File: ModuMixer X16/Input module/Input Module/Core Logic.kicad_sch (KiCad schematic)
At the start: 57 parts, among them Q1 MMBT2222A, U1 AMS1117-1.8, U2 LM324, U3 TLV320AIC3100, U4 STM32F405RGTx, U5 4016

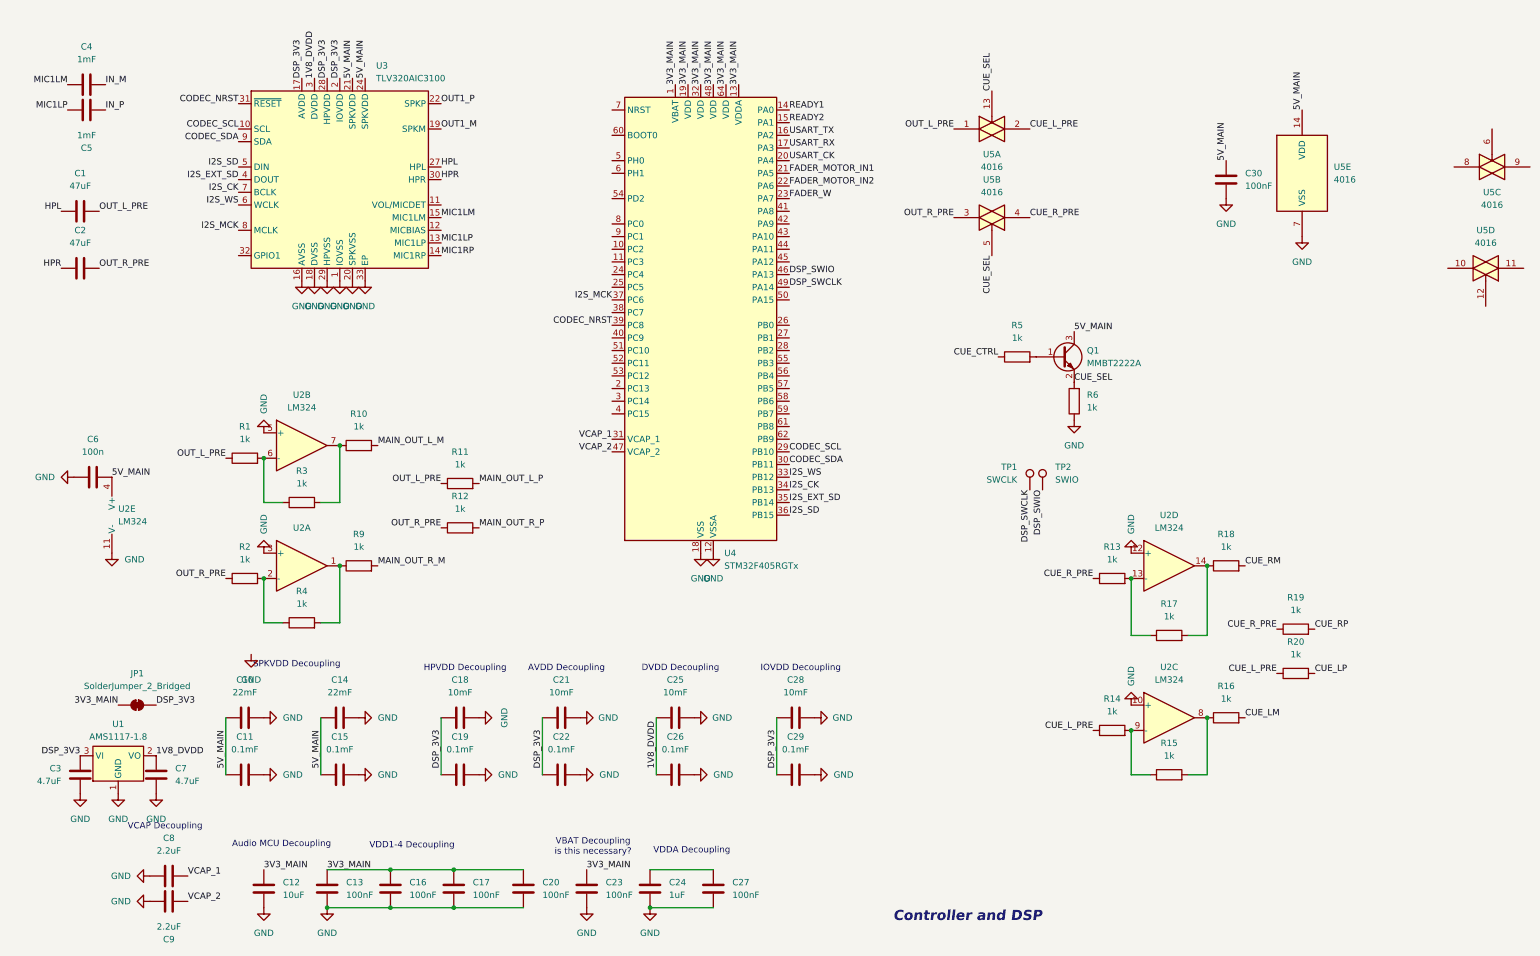
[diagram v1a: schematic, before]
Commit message: MCU replacement finished
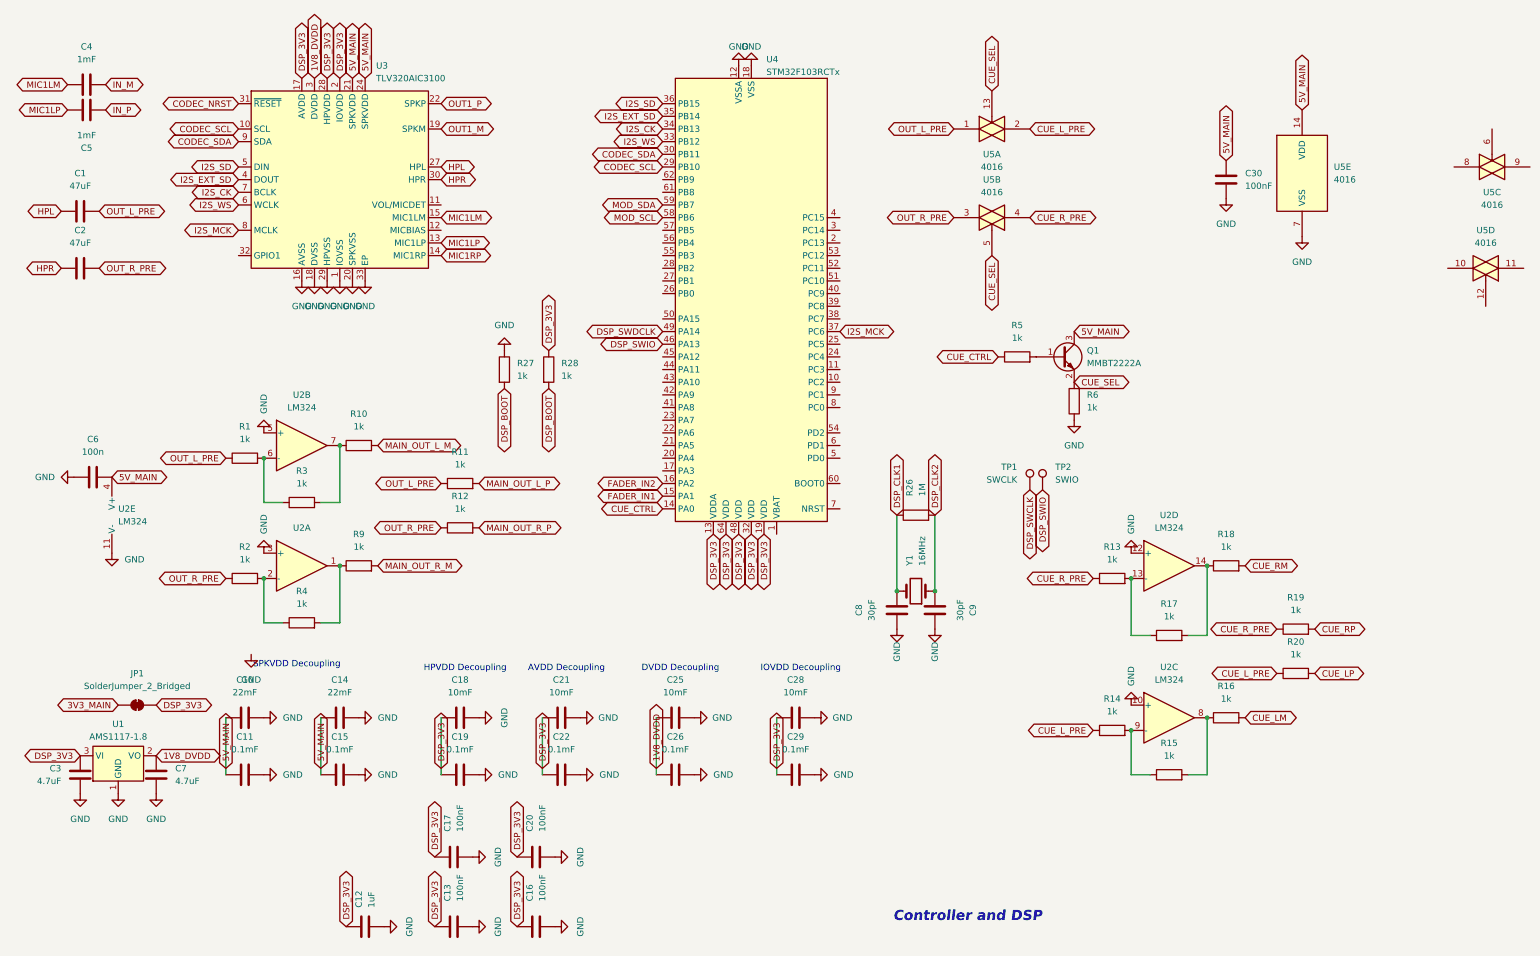
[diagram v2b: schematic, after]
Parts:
- removed C23, C27: 100nF, Capacitor_SMD:C_0603_1608Metric, symbol Device:C
- removed C24: 1uF, Capacitor_SMD:C_0603_1608Metric, symbol Device:C
- removed U4: STM32F405RGTx, Package_QFP:LQFP-64_10x10mm_P0.5mm, symbol MCU_ST_STM32F4:STM32F405RGTx
- added R26: 1M, Resistor_SMD:R_0603_1608Metric, symbol Device:R
- added R27, R28: 1k, Resistor_SMD:R_0603_1608Metric, symbol Device:R
- added U4: STM32F103RCTx, Package_QFP:LQFP-64_10x10mm_P0.5mm, symbol MCU_ST_STM32F1:STM32F103RCTx
- added Y1: 16MHz, Crystal:Crystal_HC49-U_Vertical, symbol Device:Crystal
- C12: value 10uF -> 1uF
- C8, C9: value 2.2uF -> 30pF
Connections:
- net VCAP_1 is gone; now on net GND: C8.2
- net 3V3_MAIN: no longer C12.2, C13.2, C16.2, C17.2, C20.2
- net CODEC_SCL: now also U4.29 (PB10)
- net CODEC_SDA: now also U4.30 (PB11)
- net CUE_CTRL: now also U4.14 (PA0)
- net DSP_3V3: now also C12.1, C13.1, C16.1, C17.1, C20.1, R28.1, U4.13 (VDDA), U4.19 (VDD), U4.32 (VDD), U4.48 (VDD), U4.64 (VDD)
- net DSP_SWIO: now also U4.46 (PA13)
- net GND: now also C12.2, C13.2, C16.2, C17.2, C20.2, R27.1, U4.12 (VSSA), U4.18 (VSS), U4.31 (VSS), U4.47 (VSS), U4.63 (VSS); no longer C12.1, C13.1, C16.1, C17.1, C20.1, C8.1
- net I2S_CK: now also U4.34 (PB13)
- net I2S_EXT_SD: now also U4.35 (PB14)
- net I2S_MCK: now also U4.37 (PC6)
- net I2S_SD: now also U4.36 (PB15)
- net I2S_WS: now also U4.33 (PB12)
- net VCAP_2 renamed DSP_CLK2
- net DSP_CLK2: now also R26.2, Y1.1
- new net DSP_BOOT: R27.2, R28.2
- new net DSP_CLK1: C8.1, R26.1, Y1.2
- new net DSP_SWDCLK: U4.49 (PA14)
- new net FADER_IN1: U4.15 (PA1)
- new net FADER_IN2: U4.16 (PA2)
- new net MOD_SCL: U4.58 (PB6)
- new net MOD_SDA: U4.59 (PB7)
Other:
- note removed: "Audio MCU Decoupling"
- note removed: "VBAT Decoupling is this necessary?"
- note removed: "VCAP Decoupling"
- note removed: "VDD1-4 Decoupling"
- note removed: "VDDA Decoupling"
